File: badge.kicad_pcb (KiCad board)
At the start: 2 copper layers, 68.6 x 139.7 mm, 29 parts, among them J1 DevKitC_L, J10 HT024SQV003NH, J11 EXT3, J12 DevKitC_L_SMD, J13 DevKitC_R_SMD, J2 DevKitC_R, J4 EXT1_1, J5 EXT1_2, J6 EXT1_3, J7 EXT2_1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

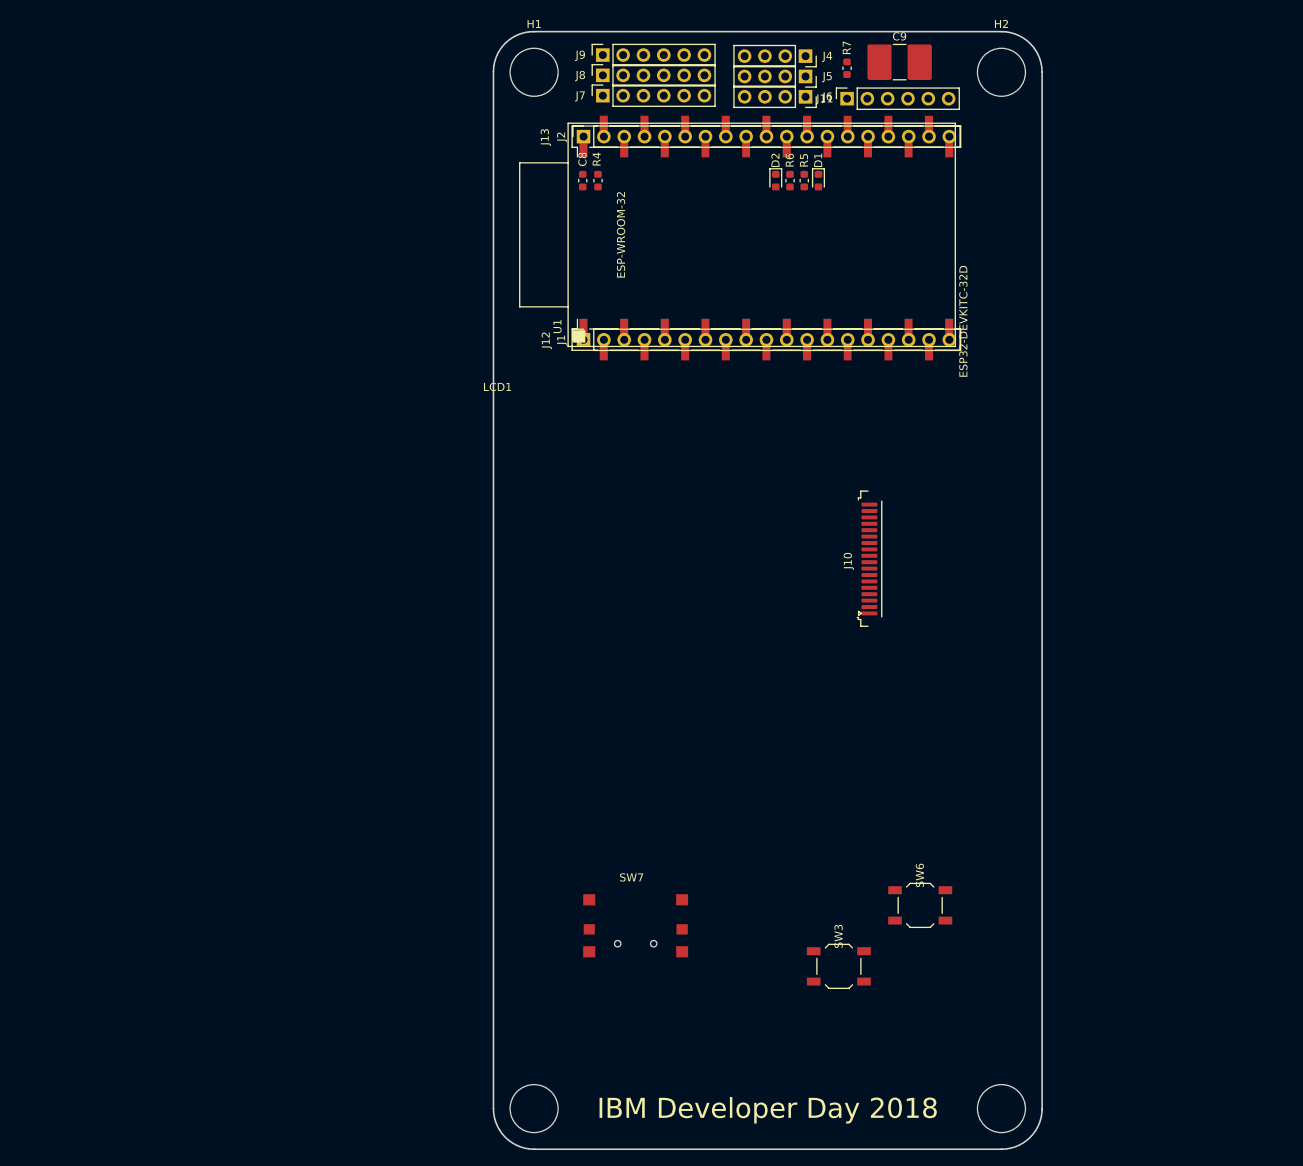
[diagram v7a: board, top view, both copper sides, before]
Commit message: Modify footprints for Silk, add IR333C
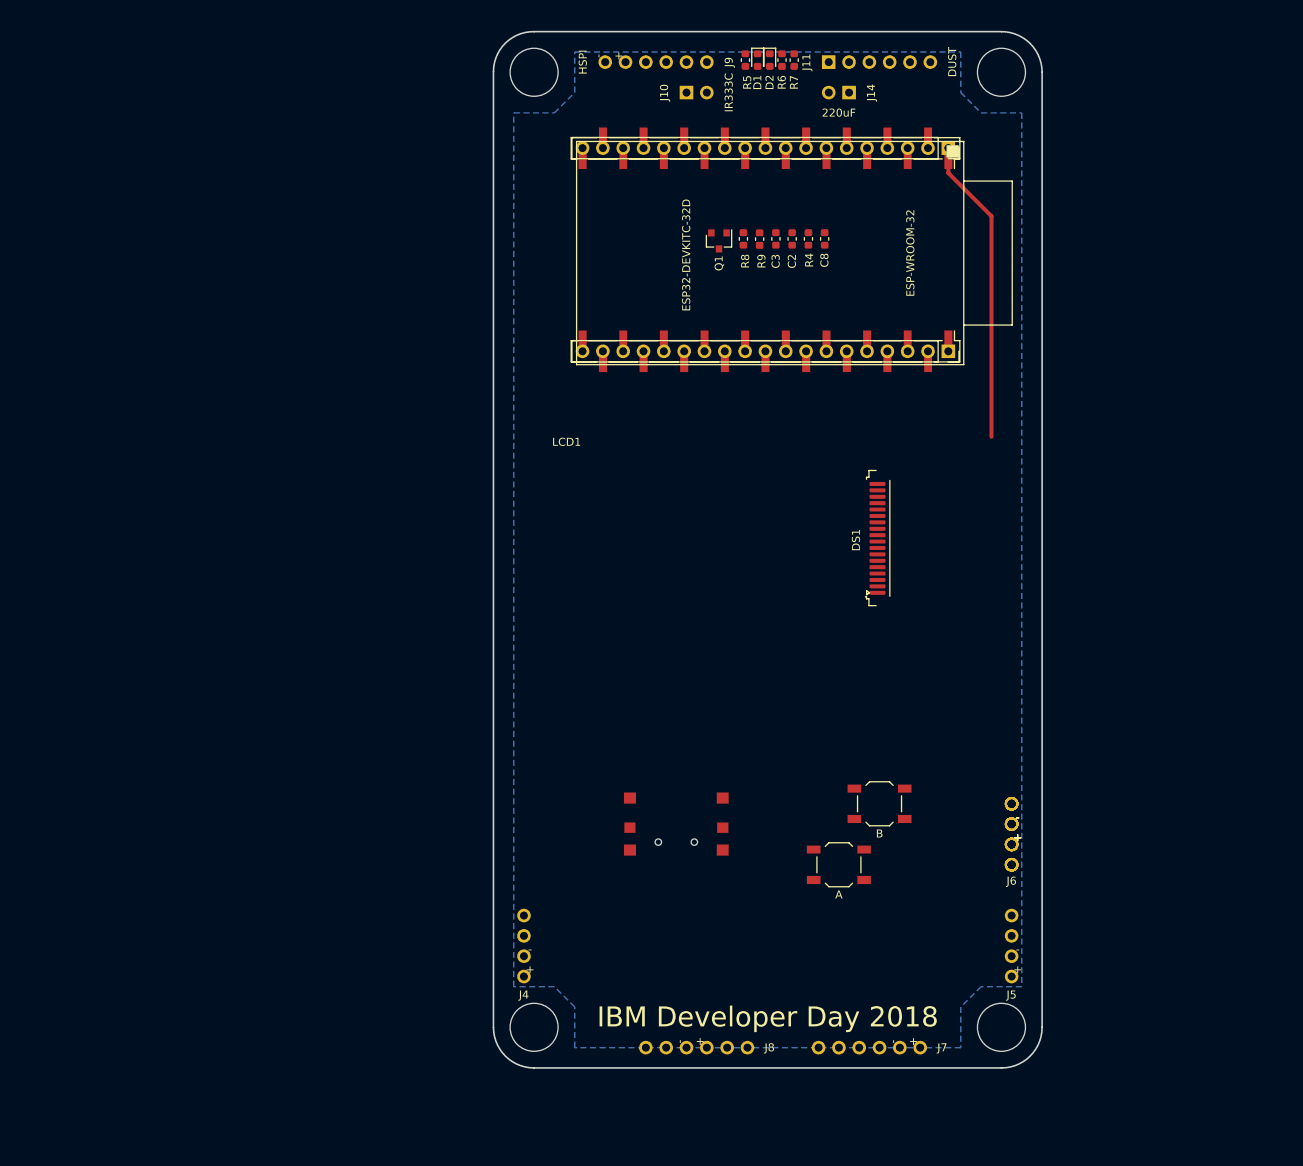
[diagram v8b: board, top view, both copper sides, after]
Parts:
- removed C9: 2917/220uF/16V, Capacitor_SMD:C_2816_7142Metric
- removed the J6 at (140.6, 20.8)
- added C2: 0603/0.1uF, Capacitor_SMD:C_0603_1608Metric, F.Cu at (138.9, 38.6)
- added C3: 0603/0.1uF, Capacitor_SMD:C_0603_1608Metric, F.Cu at (136.9, 38.6)
- added DS1: EZ240IT010, custom_footprint:COMMON_MOUNT_FFC-1x18-1MP_P0.80mm, F.Cu at (143.9, 77.8)
- added J14: 220uF, custom_footprint:PinSocket_1x02_P2.54mm_Vertical_NO3D, F.Cu at (146.1, 20.3)
- added J6 (x4): ADC_1, custom_footprint:PinSocket_1x04_P2.54mm_Vertical_NO3D_2S, F.Cu at (166.4, 116.8)
- added Q1: 2N7002, Package_TO_SOT_SMD:SOT-23, F.Cu at (129.8, 38.9)
- added R8: 0603/20R, Resistor_SMD:R_0603_1608Metric, F.Cu at (132.8, 38.6)
- added R9: 0603/36R, Resistor_SMD:R_0603_1608Metric, F.Cu at (134.9, 38.6)
- J10: value HT024SQV003NH -> IR333C; footprint custom_footprint:COMMON_MOUNT_FFC-1x18-1MP_P0.80mm -> custom_footprint:PinSocket_1x02_P2.54mm_Vertical_NO3D
- J11: value EXT3 -> DUST
- J4: value EXT1_1 -> ADC_3; footprint custom_footprint:PinSocket_1x04_P2.54mm_Vertical_NO3D -> custom_footprint:PinSocket_1x04_P2.54mm_Vertical_NO3D_1S
- J5: value EXT1_2 -> ADC_2; footprint custom_footprint:PinSocket_1x04_P2.54mm_Vertical_NO3D -> custom_footprint:PinSocket_1x04_P2.54mm_Vertical_NO3D_1S
- J7: value EXT2_1 -> DAC_1; footprint custom_footprint:PinSocket_1x06_P2.54mm_Vertical_NO3D -> custom_footprint:PinSocket_1x06_P2.54mm_Vertical_NO3D_1S
- J8: value EXT2_2 -> DAC_2; footprint custom_footprint:PinSocket_1x06_P2.54mm_Vertical_NO3D -> custom_footprint:PinSocket_1x06_P2.54mm_Vertical_NO3D_3S
- J9: value EXT2_3 -> HSPI; footprint custom_footprint:PinSocket_1x06_P2.54mm_Vertical_NO3D -> custom_footprint:PinSocket_1x06_P2.54mm_Vertical_NO3D_5S
- moved J7 125.4 mm to (154.9, 139.7), turned to 270 degrees
- moved J8 122.9 mm to (133.3, 139.7), turned to 270 degrees
- moved J4 120.3 mm to (105.4, 130.8), turned to 180 degrees
- moved J5 115.4 mm to (166.4, 130.8), turned to 180 degrees
- moved J10 62.4 mm to (125.7, 20.3)
- moved J2 52.9 mm to (158.5, 52.7), turned to 270 degrees
- moved J1 51.5 mm to (158.5, 27.3), turned to 270 degrees
- moved C8 31.1 mm to (143.0, 38.6), turned to 90 degrees
- moved R4 27.3 mm to (141.0, 38.6), turned to 90 degrees
- moved J13 26.8 mm to (135.6, 52.7), turned to 270 degrees
- moved J12 23.9 mm to (135.6, 27.3), turned to 270 degrees
- moved D1 16.9 mm to (134.6, 16.3)
- moved R5 16.8 mm to (133.1, 16.3)
- moved R6 15.1 mm to (137.7, 16.3)
- moved D2 15.1 mm to (136.1, 16.3)
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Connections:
- J10 pad 1: GND -> Net-(J10-Pad1)
- J10 pad 2: /LCD_RST -> +3V3
- J5 pad 3: /GPIO34 -> /GPIO36
- J5 pad 4: /GPIO35 -> /GPIO39
- J7 pad 3: /GPIO27 -> /GPIO26
- J7 pad 4: /GPIO26 -> /GPIO25
- J7 pad 5: /GPIO25 -> /GPIO33
- J7 pad 6: /GPIO33 -> /GPIO27
- J8 pad 1: +3V3 -> /GPIO27
- J8 pad 2: GND -> /GPIO25
- J8 pad 3: /GPIO27 -> +3V3
- J8 pad 4: /GPIO26 -> GND
- J8 pad 5: /GPIO25 -> /GPIO33
- J8 pad 6: /GPIO33 -> /GPIO26
- J9 pad 3: /GPIO27 -> /GPIO14
- J9 pad 4: /GPIO26 -> /GPIO12
- J9 pad 5: /GPIO25 -> /GPIO13
- J9 pad 6: /GPIO33 -> /GPIO15
- R4 pad 1: Net-(J10-Pad11) -> Net-(DS1-Pad11)
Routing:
- net +3V3: track 0.00 -> 38.3 mm
- net GND: track 0.00 -> 4.95 mm
- net /GPIO36: track 0.00 -> 1.68 mm
- net /GPIO34: track 0.00 -> 1.68 mm
- net /GPIO32: track 0.00 -> 1.68 mm
- net /GPIO27: track 0.00 -> 1.68 mm
- net /GPIO25: track 0.00 -> 1.68 mm
- net /GPIO13: track 0.00 -> 1.68 mm
- net /GPIO12: track 0.00 -> 1.68 mm
- net +5V: track 0.00 -> 1.68 mm
- net /VSPI_SCK: track 0.00 -> 1.66 mm
- net /LCD_DC: track 0.00 -> 1.66 mm
- net /GPIO4: track 0.00 -> 1.66 mm
- net /GPIO2: track 0.00 -> 1.66 mm
- net /GPIO17: track 0.00 -> 1.66 mm
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- added copper zone on B.Cu, net GND
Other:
- board size 68.6 x 139.7 mm -> 68.6 x 129.5 mm
- net class Default: clearance 0.2 -> 0.5; trace_width 0.3 -> 0.5
- net class Touch trace added: clearance 0.5, trace_width 0.18, via_dia 0.8, via_drill 0.4
- rule trace_clearance: 0.2 -> 0.5
- rule trace_min: 0.2 -> 0.15
